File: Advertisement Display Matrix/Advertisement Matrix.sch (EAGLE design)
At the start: 27 parts, among them IC1 MAX7219CNG, IC2 74HC540N, IC3 UDN2981A, IC9 ATMEGA168-20P, Y3 16Mhz

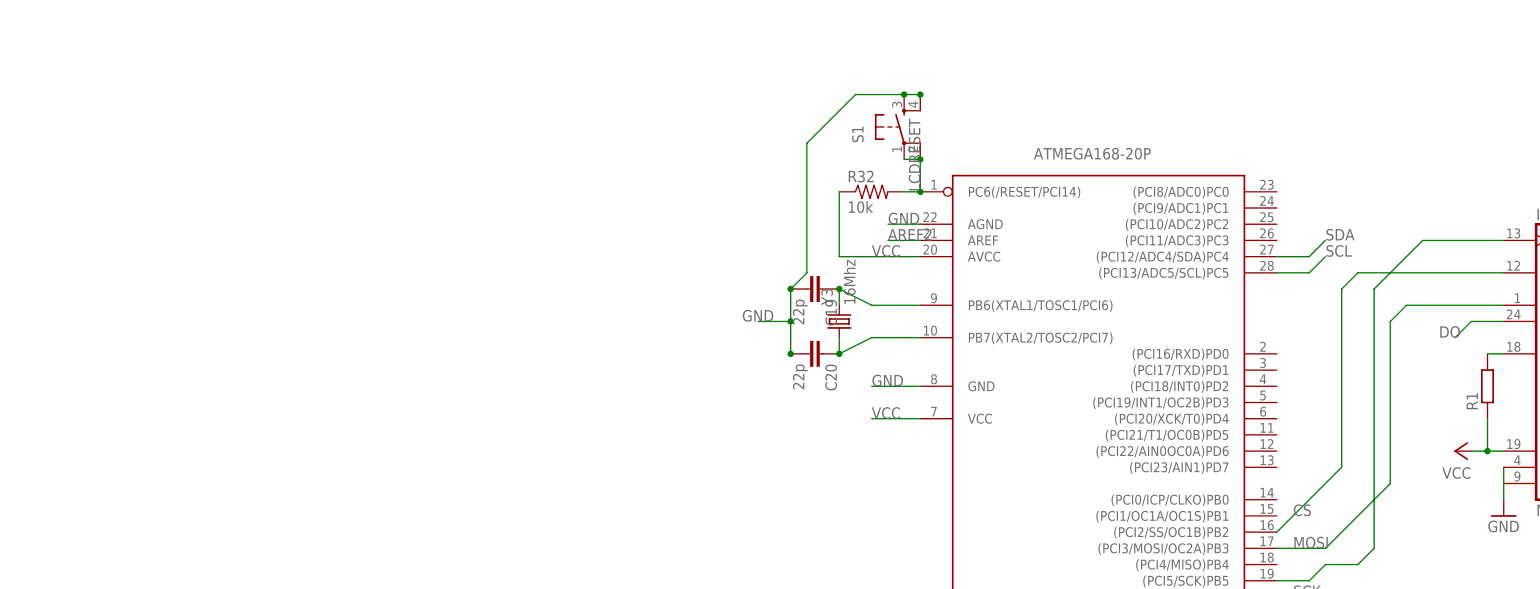
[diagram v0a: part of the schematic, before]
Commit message: Tiny-TinyG, Plus gerbers of Reflow and Advertisement
Started new project: TinyTinyG
Generated Gerbers for Advertisement Display driver and ReflowOvenShield
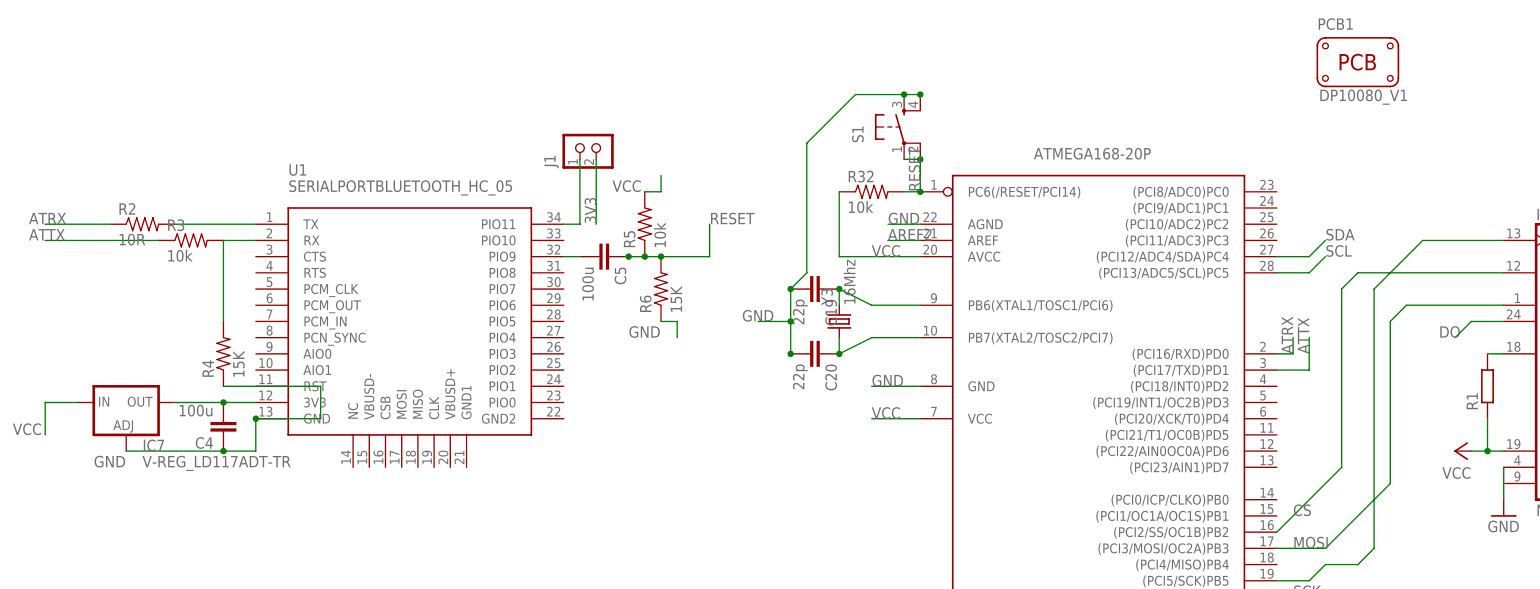
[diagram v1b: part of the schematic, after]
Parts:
- added C4, C5: 100u, SparkFun-Passives:CAP1206
- added IC7: V-REG_LD117ADT-TR, untitled:V-REG_LD117ADT-TR
- added J1: CON_HEADER_1X02-PTH, dp_devices:CON_HEADER_1X02-PTH
- added PCB1: PCB_DP_RECTANGLE-80X100, dp_devices:PCB_DP_RECTANGLE-80X100
- added R2: 10R, resistor:R-US_M1206
- added R3, R5: 10k, resistor:R-US_M1206
- added R4, R6: 15K, resistor:R-US_M1206
- added U1: SERIALPORTBLUETOOTH_HC_05, untitled:SERIALPORTBLUETOOTH_HC_05
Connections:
- removed net LCDRESET: IC9.PC6(/RESET/PCI14), R32.2, S1.1, S1.2
- new net 3V3: C4.2, IC7.OUT, J1.2, U1.3V3
- new net ATRX: IC9.(PCI16/RXD)PD0, R2.1
- new net ATTX: IC9.(PCI17/TXD)PD1, R3.1
- new net N$43: R2.2, U1.TX
- new net N$44: R3.2, R4.2, U1.RX
- new net N$45: J1.1, U1.PIO11
- new net N$47: C5.2, U1.PIO9
- new net RESET: C5.1, IC9.PC6(/RESET/PCI14), R32.2, R5.1, R6.2, S1.1, S1.2
- net GND: now also C4.1, IC7.ADJ, R4.1, R6.1, U1.GND
- net VCC: now also IC7.IN, R5.2
